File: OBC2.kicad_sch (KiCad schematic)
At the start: 80 parts, among them IC1 LTC4411, IC2 LTC4411, J1 Conn_02x30_Row_Letter_First, J2 Conn_02x30_Row_Letter_First, J3 USB_B, J4 8P8C_Shielded, J5 FTSH-107-01-F-DV-K, U1 USBLC6-2SC6, U2 R-783.3-0.5, U3 STM32F407VETx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

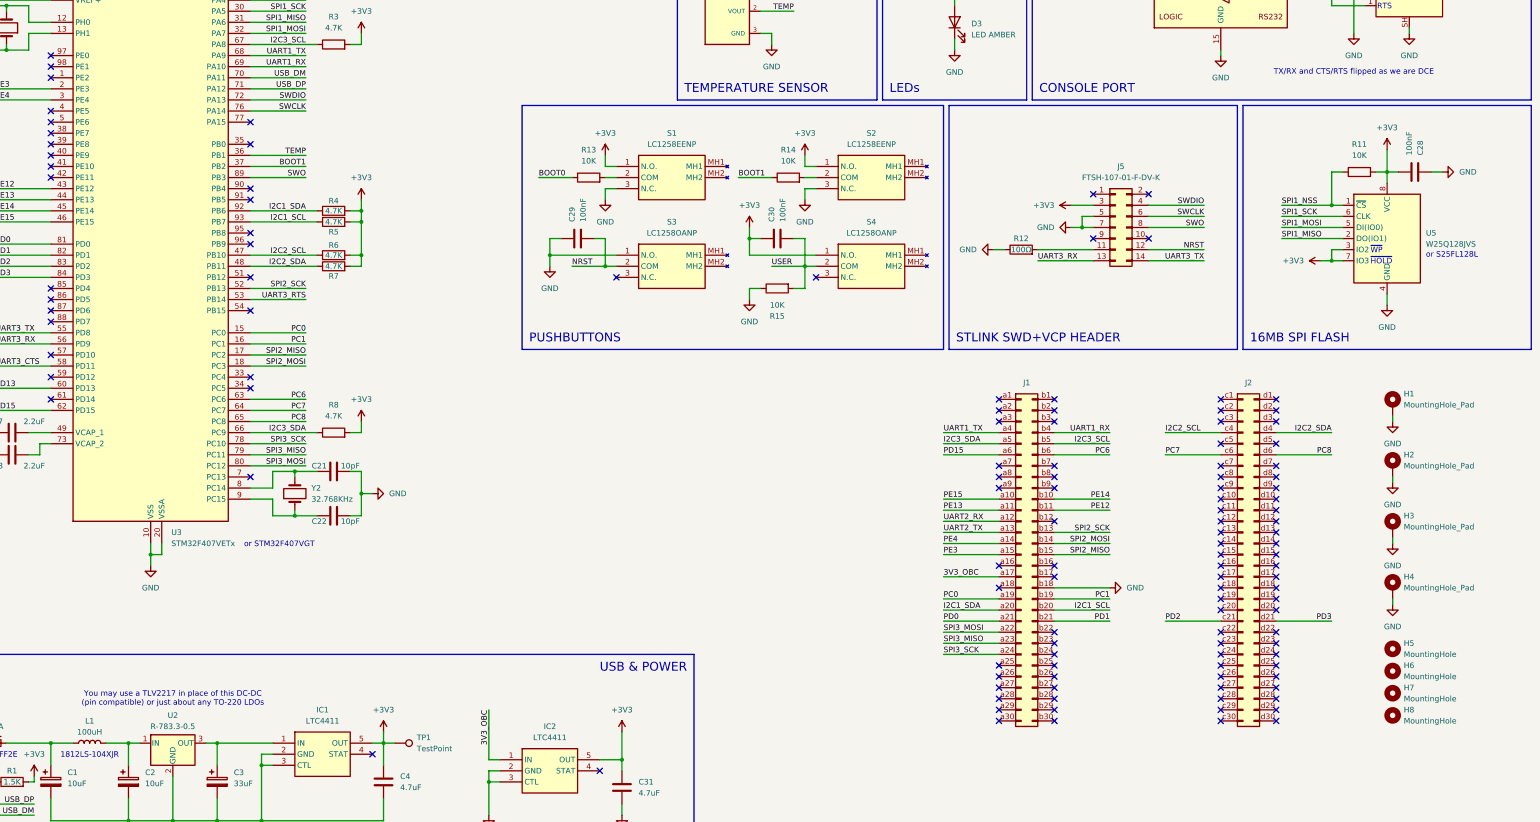
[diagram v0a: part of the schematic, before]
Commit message: correct flipped i2c1 SCL SDA lines
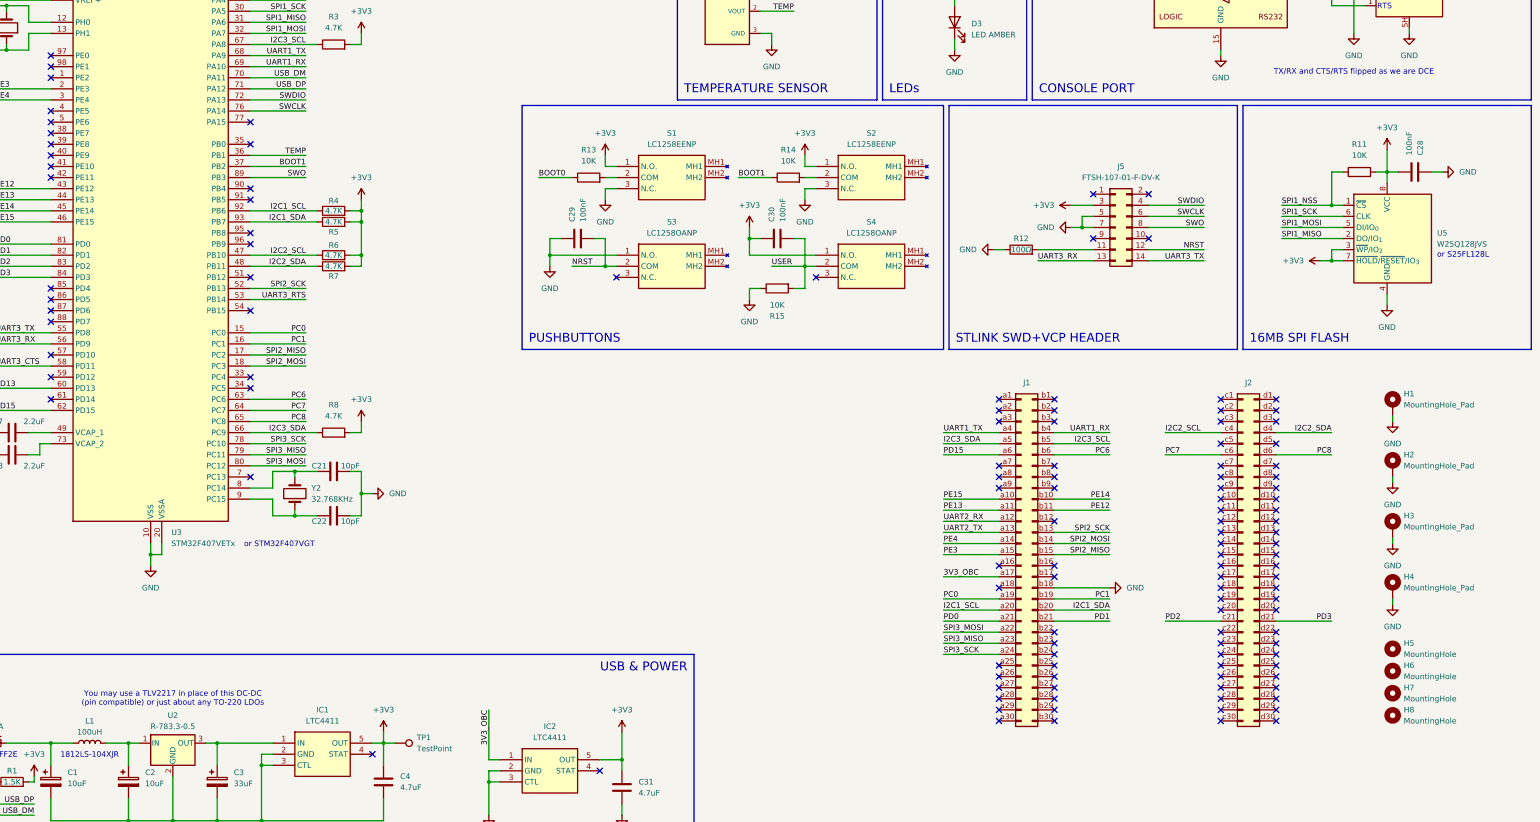
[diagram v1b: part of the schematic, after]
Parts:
- U5: footprint Package_SO:SOIC-8_5.23x5.23mm_P1.27mm -> Package_SO:SOIC-8_5.3x5.3mm_P1.27mm
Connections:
- net I2C1_SCL: now also J1.a20 (Pin_a20), R4.1, U3.92 (PB6); no longer J1.b20 (Pin_b20), R5.1, U3.93 (PB7)
- net I2C1_SDA: now also J1.b20 (Pin_b20), R5.1, U3.93 (PB7); no longer J1.a20 (Pin_a20), R4.1, U3.92 (PB6)
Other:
- note removed: "~{HOLD}"
- note removed: "~{WP}"
- moved on the sheet: U5
